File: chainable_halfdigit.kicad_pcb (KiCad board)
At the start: 2 copper layers, 100 x 100 mm, 60 parts, among them J1 Conn_01x03, J2 Conn_01x03

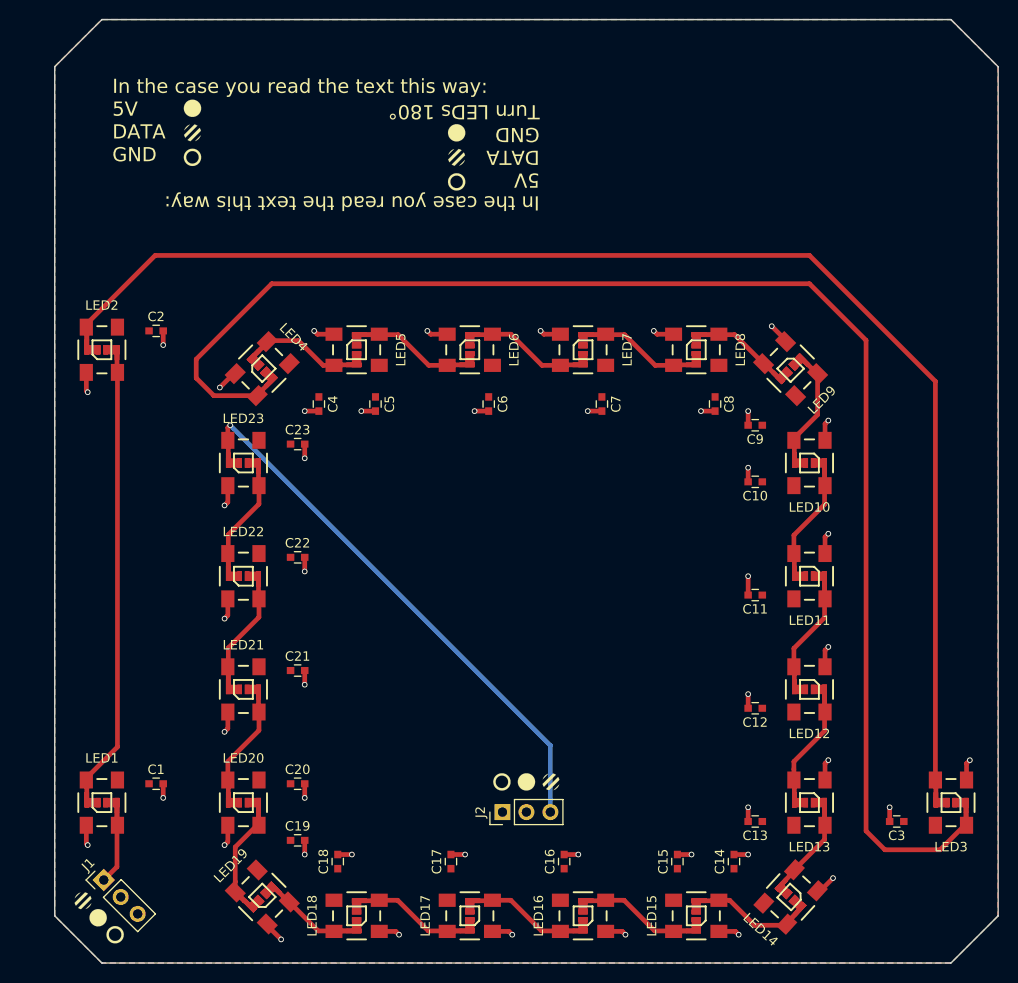
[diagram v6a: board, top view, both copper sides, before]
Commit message: Moved connectors and capacitors on back layer
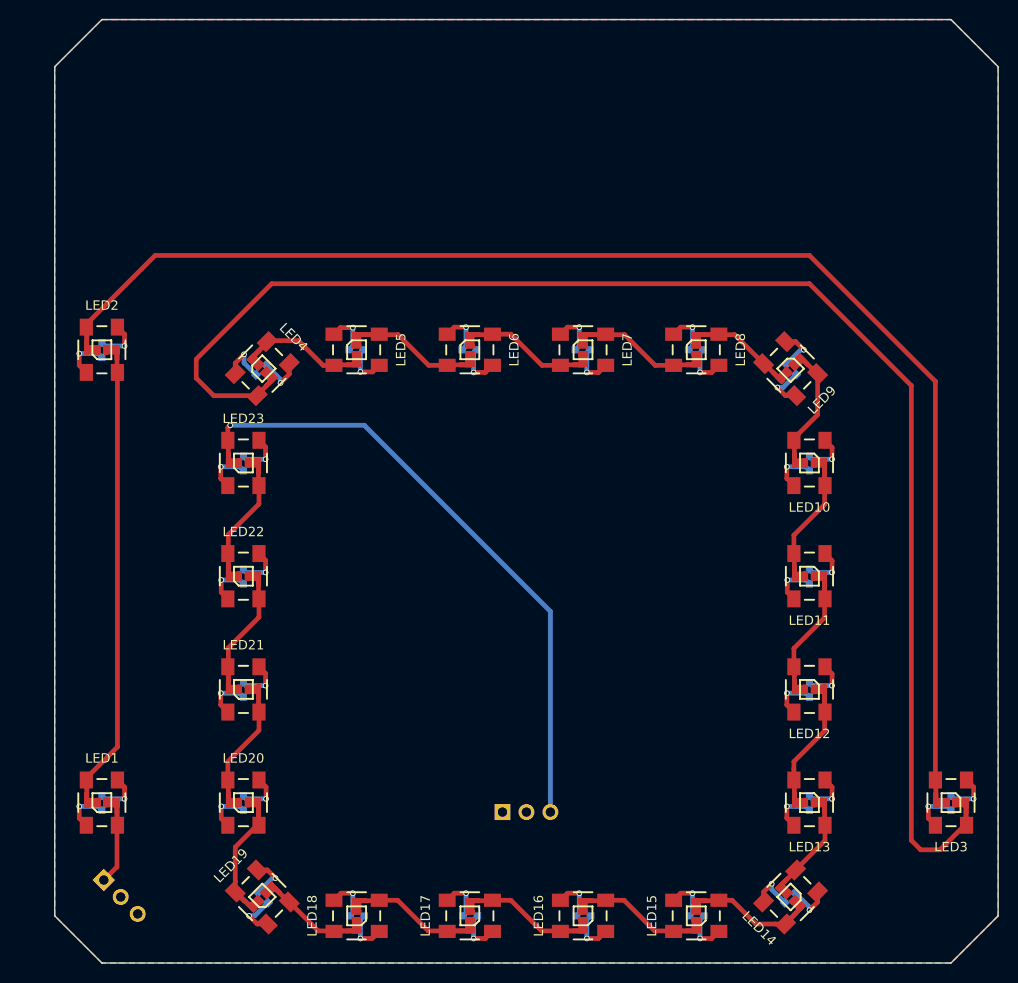
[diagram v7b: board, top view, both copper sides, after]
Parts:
- C1, C10, C11, C12, C13, C14, C15, C16, C17, C18, C19, C2, C20, C21, C22, C23, C3, C4, C5, C6, C7, C8, C9, G*** (x12), J1, J2: moved to B.Cu
- moved C4 7.12 mm to (111.9, 87.1), turned to 225 degrees
- moved C19 7.10 mm to (112.1, 143.1), turned to 315 degrees
- moved C14 7.05 mm to (167.9, 143.1), turned to 45 degrees
- moved C9 7.05 mm to (168.1, 87.1), turned to 135 degrees
- moved G*** 6.60 mm to (137.4, 137.4)
- moved G*** 6.60 mm to (142.6, 137.4)
- moved G*** 6.60 mm to (140.0, 137.4)
- moved G*** 6.26 mm to (110.2, 67.4)
- moved G*** 6.26 mm to (110.2, 62.2)
- moved G*** 6.26 mm to (110.2, 64.8)
- moved C1 6.10 mm to (95.0, 133.1), turned to 270 degrees
- moved C15 6.10 mm to (158.1, 145.0), turned to 0 degrees
- moved C16 6.10 mm to (146.1, 145.0), turned to 0 degrees
- moved C17 6.10 mm to (134.1, 145.0), turned to 0 degrees
- moved C20 6.10 mm to (110.0, 133.1), turned to 270 degrees
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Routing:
- net 5V: track 0.00 -> 111.2 mm, vias 0 -> 23
- net GND: track 86.4 -> 112.1 mm, vias 46 -> 23
- net DATA_OUT: track 56.8 -> 65.1 mm
- net Net-(LED3-Pad2): track 151.9 -> 149.6 mm
- net Net-(LED13-Pad2): track 7.44 -> 6.03 mm
